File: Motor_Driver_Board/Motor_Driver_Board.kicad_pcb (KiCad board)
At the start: 2 copper layers, 63.8 x 52.5 mm, 33 parts, among them J1 POWER, J2 MOTOR, J3 LCD, SW1 ENCODER, U1 XL1509-5.0

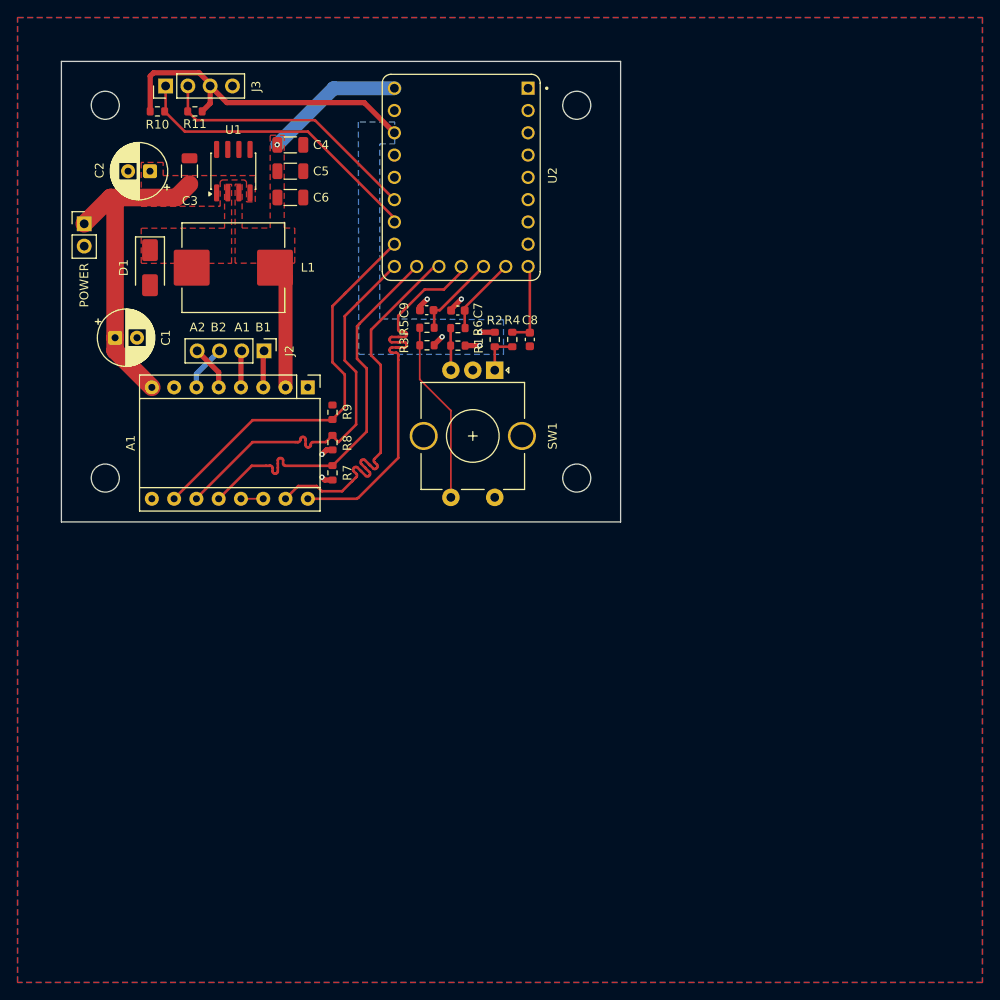
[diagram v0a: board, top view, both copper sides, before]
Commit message: Layout revision
Updated the schematic pinout for the RP2040.
Updated the PCB layout.
Rotated the motor driver.
Moved the motor header to the side of the board.
Added via stitching.
Removed vias in pads.
Removed length matching from traces.
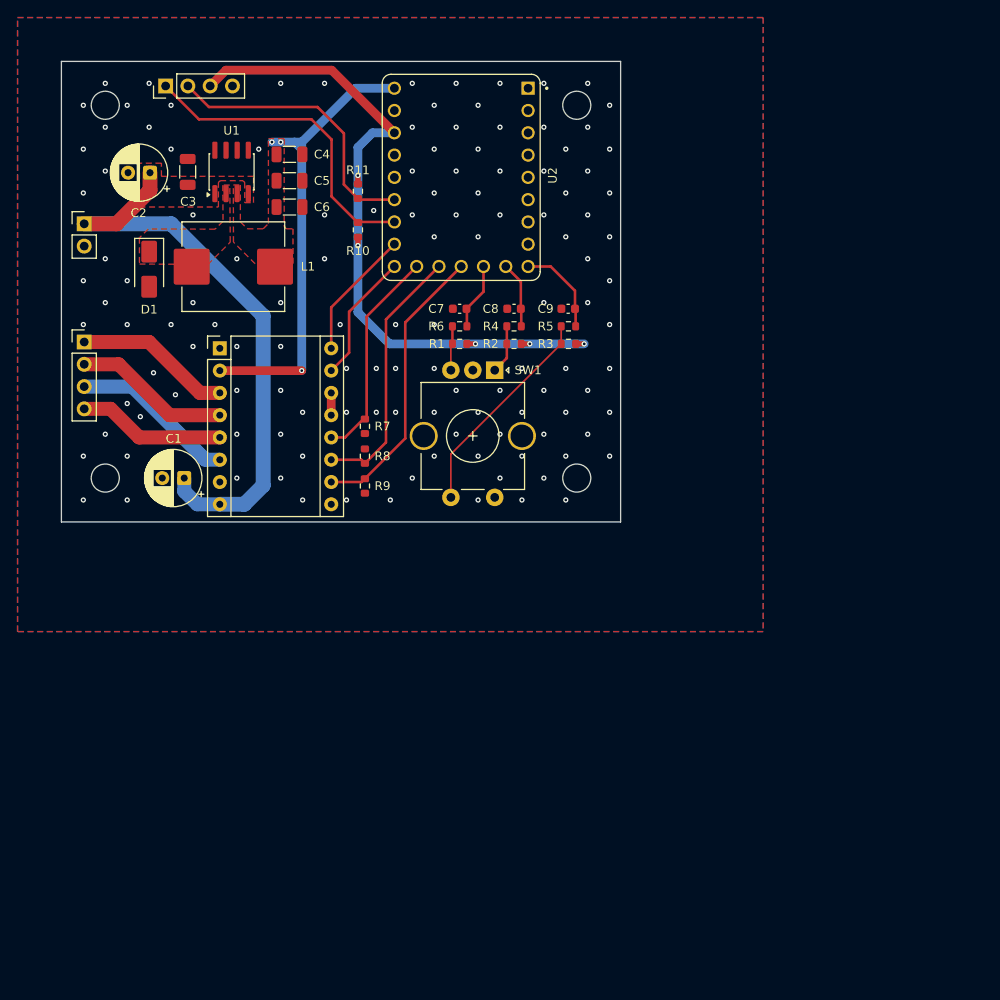
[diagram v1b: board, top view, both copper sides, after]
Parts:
- moved R10 26.5 mm to (96.1, 53.8), turned to 90 degrees
- moved R11 20.7 mm to (96.1, 49.4), turned to -90 degrees
- moved J2 20.5 mm to (64.9, 66.6), turned to 0 degrees
- moved C1 17.8 mm to (76.3, 82.1), turned to 180 degrees
- moved C9 16.1 mm to (120.1, 62.8)
- moved R3 16.1 mm to (120.1, 66.8)
- moved R5 16.1 mm to (120.1, 64.8)
- moved A1 11.0 mm to (80.4, 67.3), turned to 0 degrees
- moved R9 9.18 mm to (96.9, 83.0), turned to -90 degrees
- moved R7 6.46 mm to (96.9, 76.2)
- moved R8 4.01 mm to (96.9, 79.6), turned to 90 degrees
- moved C8 3.94 mm to (113.9, 62.8), turned to 180 degrees
- moved R2 2.26 mm to (113.9, 66.8), turned to 180 degrees
- moved R4 1.51 mm to (113.9, 64.8), turned to 0 degrees
- moved C4 1.09 mm to (88.3, 45.2)
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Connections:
- U2 pad 10: /ENC_CW -> /ENC_CC
- U2 pad 11: /ENC_SW -> /ENC_CW
- U2 pad 12: /DIR -> /MS1
- U2 pad 13: /STEP -> /MS2
- U2 pad 15: /MS2 -> /STEP
- U2 pad 16: /MS1 -> /DIR
- U2 pad 9: /ENC_CC -> /ENC_SW
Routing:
- net +3V3: track 43.0 -> 80.5 mm, vias 3 -> 5
- net /STEP: track 45.0 -> 14.9 mm
- net /DIR: track 44.9 -> 14.9 mm
- net VCC: track 37.5 -> 67.2 mm
- net +5V: track 30.2 -> 53.0 mm, vias 1 -> 3
- net /MS3: track 45.0 -> 24.1 mm
- net /MS2: track 45.0 -> 30.0 mm
- net /B1: track 4.20 -> 17.9 mm
- net /A1: track 4.20 -> 17.9 mm
- net /B2: track 5.25 -> 18.9 mm
- net /MS1: track 45.9 -> 32.7 mm
- net /A2: track 5.17 -> 16.8 mm
- net GND: track 6.14 -> 0.00 mm, vias 4 -> 132
- net Net-(R3-Pad2): track 20.8 -> 24.7 mm
- net /ENC_CC: track 9.65 -> 7.48 mm
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- removed copper zone on B.Cu, net +3V3
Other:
- board text removed: "A1"
- board text removed: "A2"
- board text removed: "B1"
- board text removed: "B2"

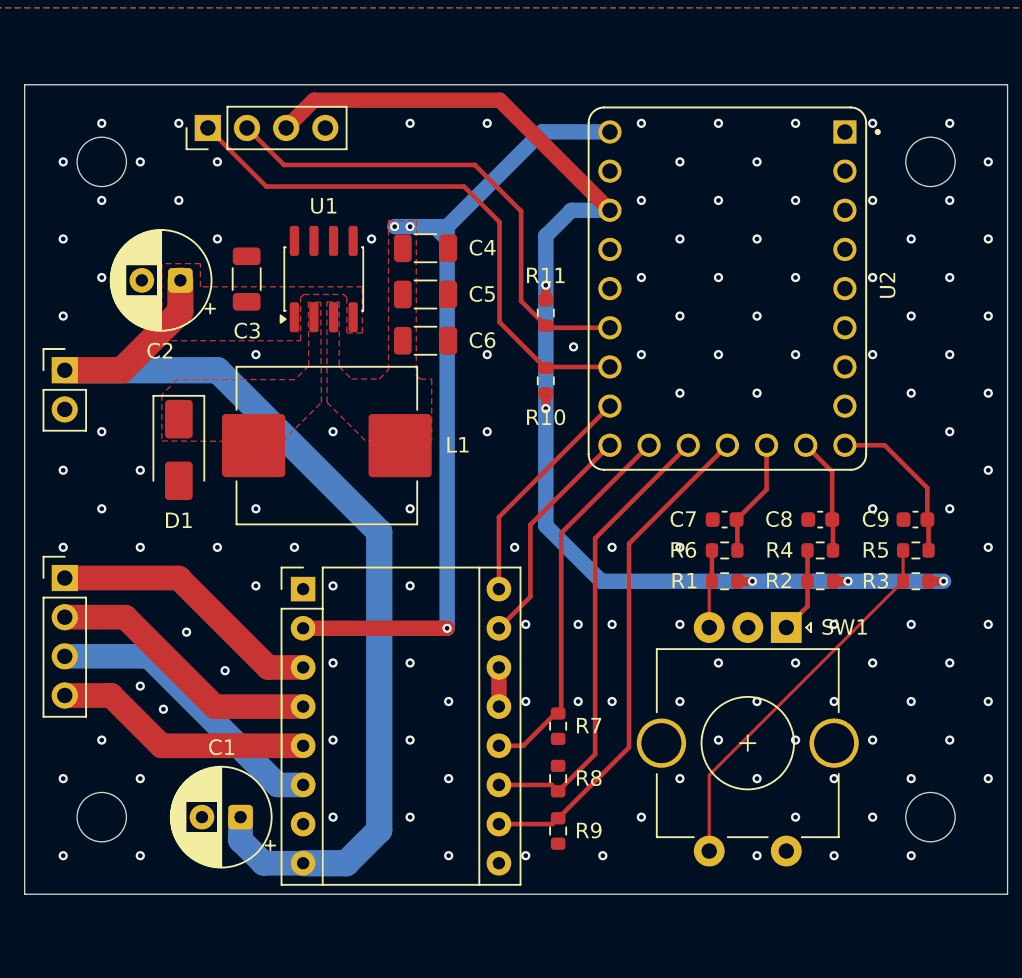
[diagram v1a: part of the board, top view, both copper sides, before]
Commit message: PCB layout and models
Updated the PCB layout.
Updated the models for the MCU, motor driver and encoder.
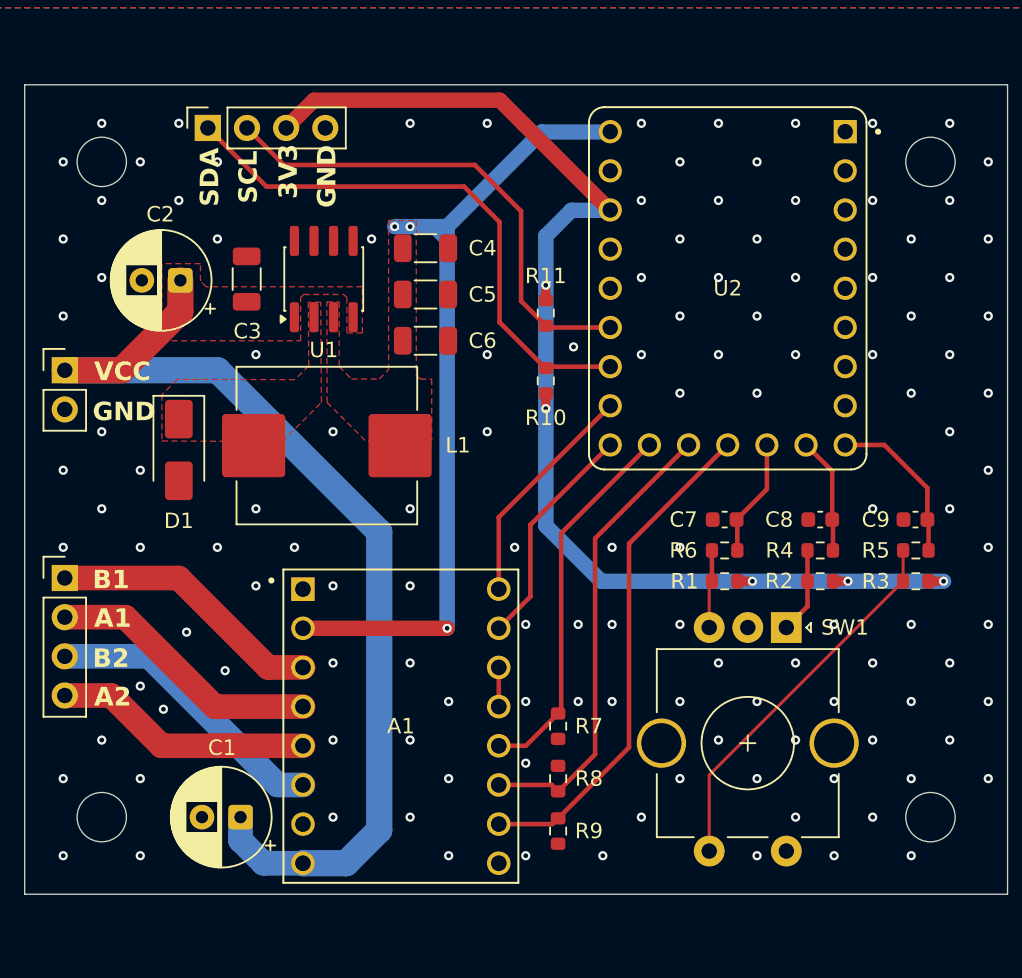
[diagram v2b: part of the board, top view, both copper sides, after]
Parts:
- A1: footprint Module:Pololu_Breakout-16_15.2x20.3mm -> Custom_Parts:MODULE_A4988_STEPPER_MOTOR_DRIVER_CARRIER
- J3: footprint Connector_PinHeader_2.54mm:PinHeader_1x04_P2.54mm_Vertical -> Connector_PinSocket_2.54mm:PinSocket_1x04_P2.54mm_Vertical
- SW1: footprint Rotary_Encoder:RotaryEncoder_Alps_EC11E-Switch_Vertical_H20mm_CircularMountingHoles -> Custom_Parts:RotaryEncoder_Alps_EC11E
- U2: footprint RP2040Zero:MODULE_RP2040-ZERO -> Custom_Parts:MODULE_RP2040-ZERO
- moved A1 10.9 mm to (86.7, 76.2)
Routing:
- net GND: vias 132 -> 133
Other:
- board text added: "3V3"
- board text added: "A1"
- board text added: "A2"
- board text added: "B1"
- board text added: "B2"
- board text added: "GND"
- board text added: "SCL"
- board text added: "SDA"
- board text added: "VCC"

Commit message: Silkscreen notes
Added some notes to the silkscreen layer.
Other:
- board text added: "MOTOR DRIVER"
- board text added: "V1.0 REV A PD 05/26 RYAN WANG DAVID MT"

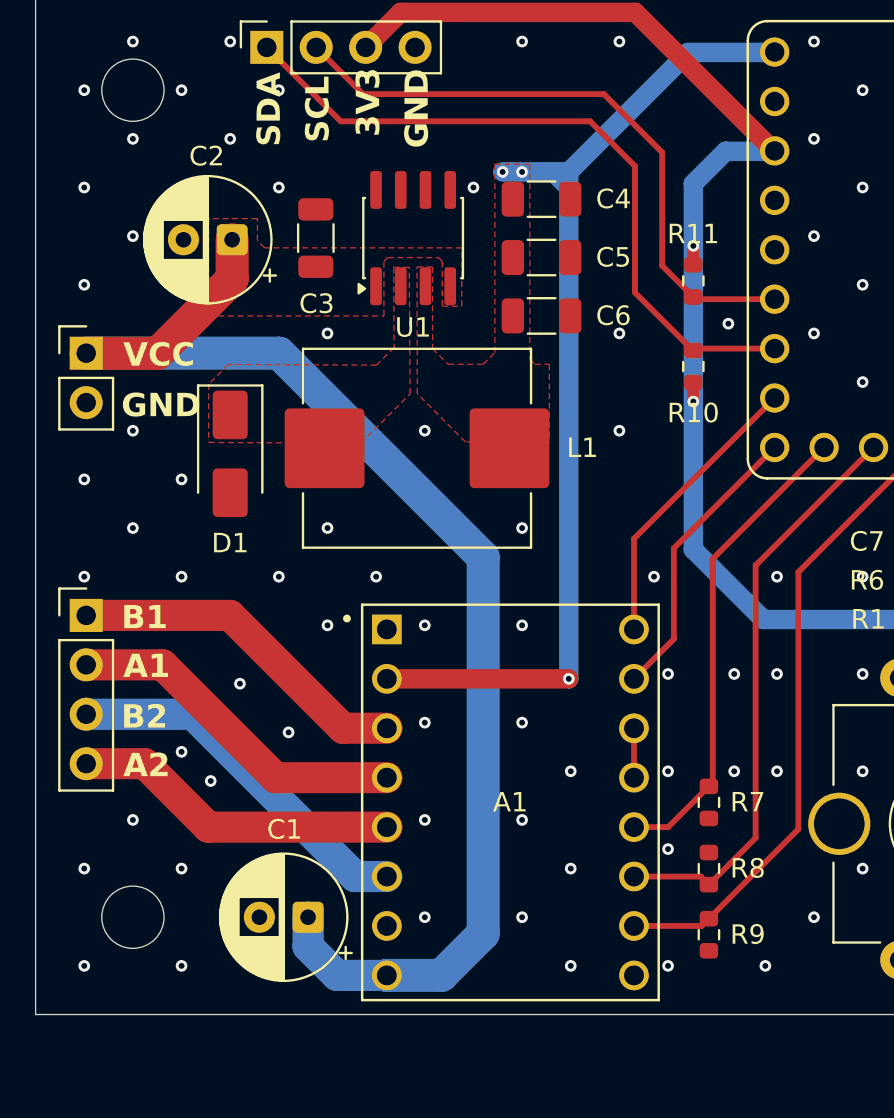
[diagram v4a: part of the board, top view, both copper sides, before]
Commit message: Footprints
Updated the footprint for the bulk capacitors.
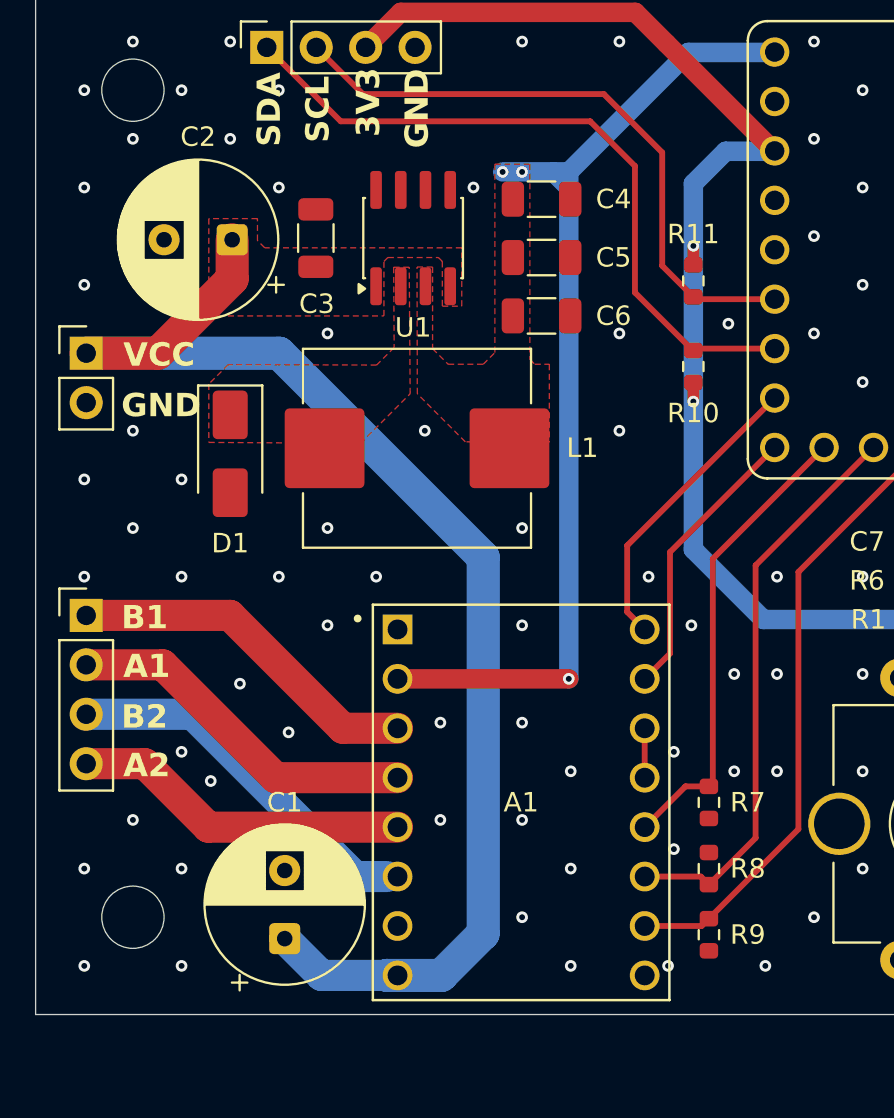
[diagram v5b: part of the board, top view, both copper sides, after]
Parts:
- C1, C2: footprint Capacitor_THT:CP_Radial_D6.3mm_P2.50mm -> Capacitor_THT:CP_Radial_D8.0mm_P3.50mm
- moved C1 1.63 mm to (75.1, 83.2), turned to 90 degrees
- moved A1 0.55 mm to (87.3, 76.2)
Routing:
- net /MS2: track 30.0 -> 29.4 mm
- net /B1: track 17.9 -> 18.4 mm
- net /A2: track 16.8 -> 17.4 mm
- net /A1: track 17.9 -> 18.4 mm
- net +5V: track 53.0 -> 52.5 mm
- net /DIR: track 14.9 -> 15.4 mm
- net GND: vias 133 -> 129

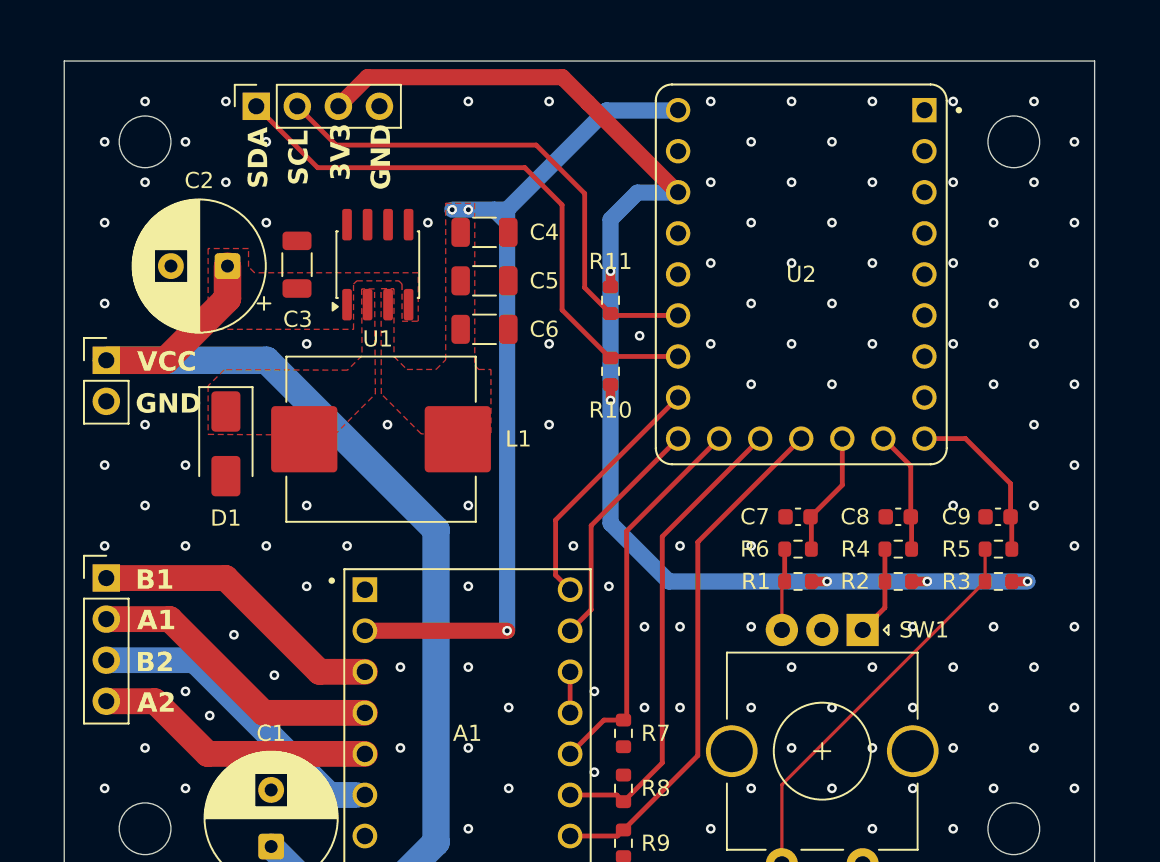
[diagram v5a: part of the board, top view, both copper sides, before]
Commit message: Tooling and silkscreen
Updated the silkscreen.
Added tooling holes for the assembly service.
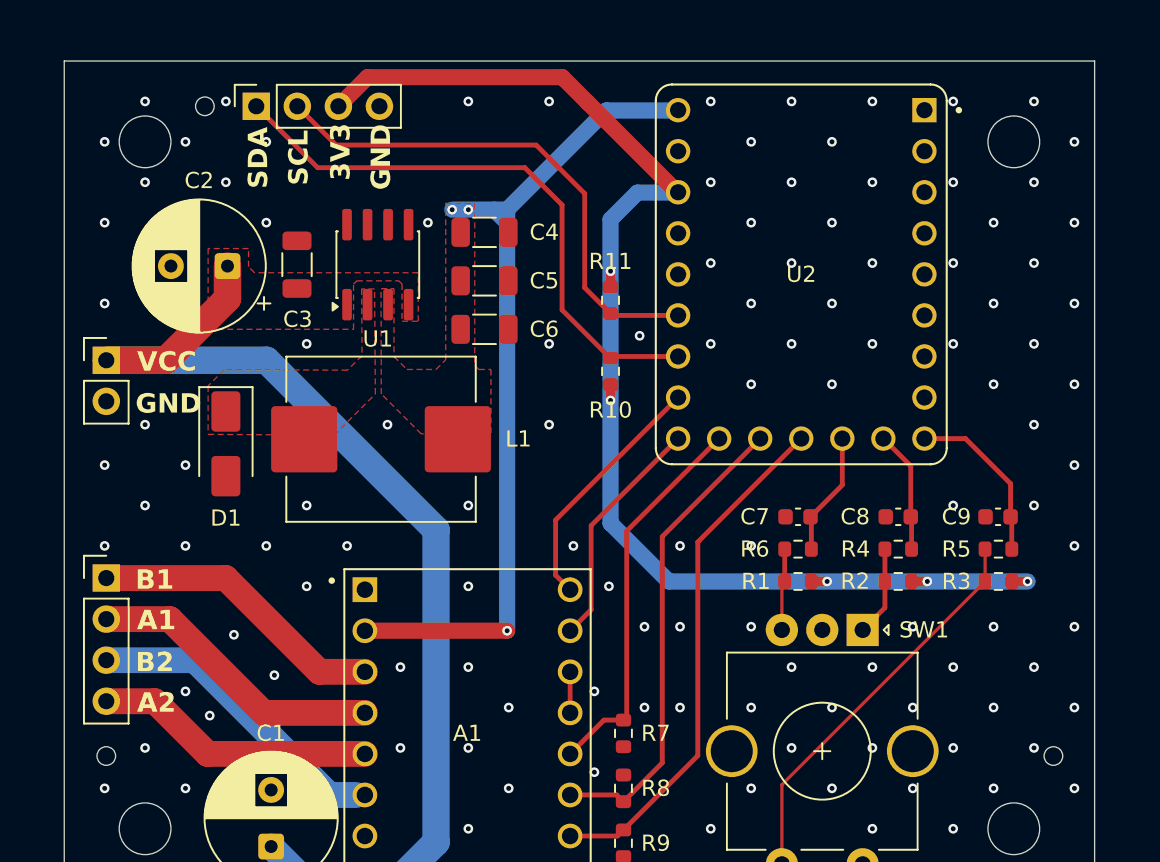
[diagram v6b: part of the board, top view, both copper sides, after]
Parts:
- added H5: TOOL, MountingHole:ToolingHole_1.152mm, F.Cu at (71.0, 37.4)
- added H6: TOOL, MountingHole:ToolingHole_1.152mm, F.Cu at (123.5, 77.6)
- added H7: TOOL, MountingHole:ToolingHole_1.152mm, F.Cu at (64.9, 77.6)
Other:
- board text added: "INTEGRATED SYSTEMS LABORATORY WASEDA"
